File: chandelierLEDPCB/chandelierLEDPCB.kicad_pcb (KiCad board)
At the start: 2 copper layers, 100 x 100 mm, 122 parts, among them J1 JST PH 1x02 SMT VERT, J3 JST PH 1x02 SMT VERT, Q1 Si2301CDS, Q10 Si2301CDS, Q11 Si2301CDS, Q12 Si2301CDS, Q13 Si2301CDS, Q14 Si2301CDS, Q15 Si2301CDS, Q16 Si2301CDS, Q17 Si2301CDS, Q18 Si2301CDS, Q19 Si2301CDS, Q2 Si2301CDS, Q20 Si2301CDS, Q21 Si2301CDS, Q22 Si2301CDS, Q23 Si2301CDS, Q24 Si2301CDS, Q3 Si2301CDS, Q4 Si2301CDS, Q5 Si2301CDS, Q6 Si2301CDS, Q7 Si2301CDS, Q8 Si2301CDS, Q9 Si2301CDS, U1 WS2811, U2 WS2811, U3 WS2811, U4 WS2811, U5 WS2811, U6 WS2811, U7 WS2811, U8 WS2811

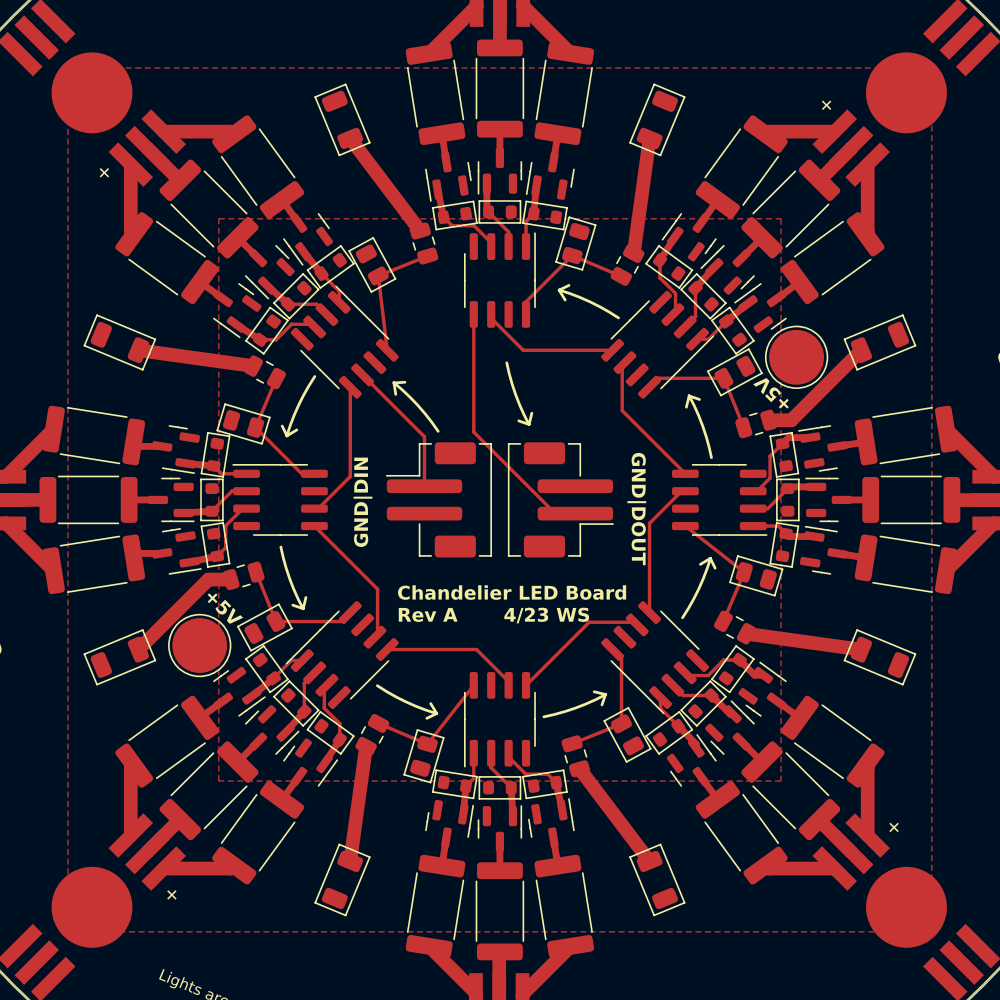
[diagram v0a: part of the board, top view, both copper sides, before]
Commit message: Edited LED to have EP disconnected
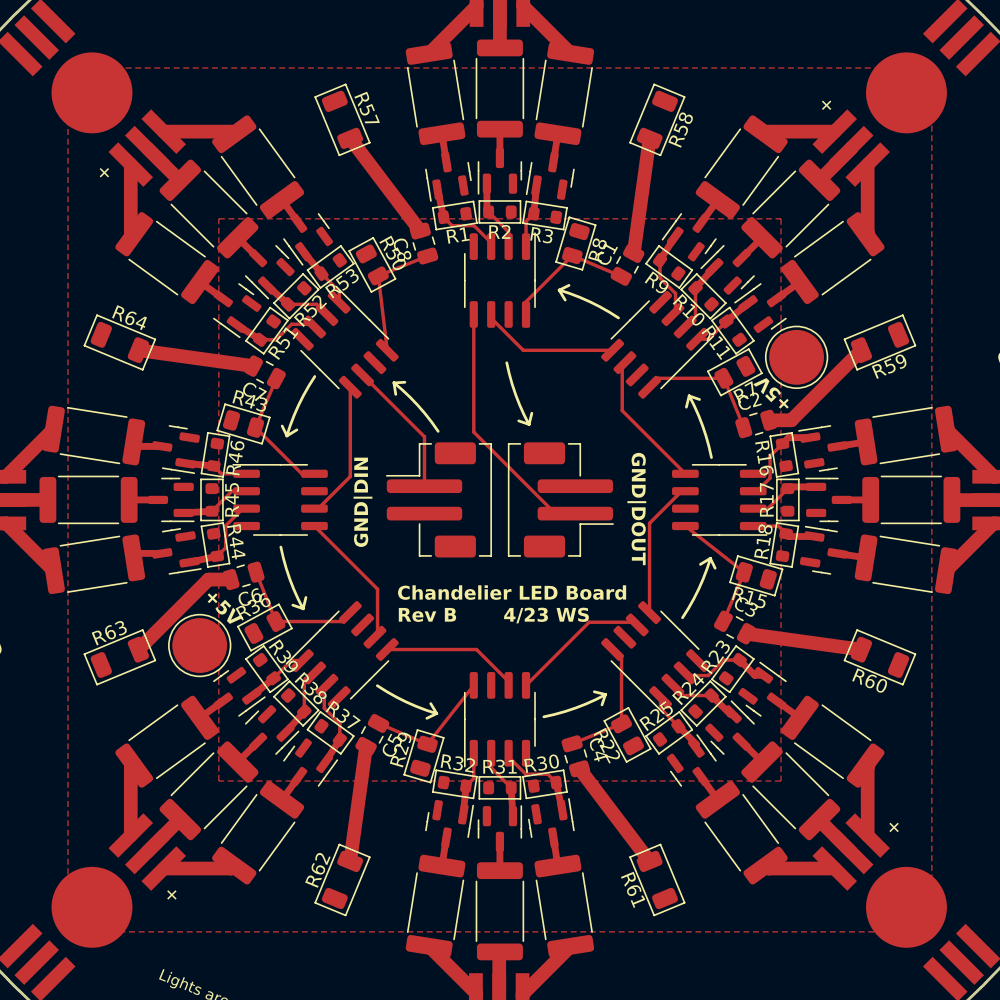
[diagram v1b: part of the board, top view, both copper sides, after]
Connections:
- D1 pad 7: GNDPWR -> unconnected-(D1-PAD-Pad7)
- D2 pad 7: GNDPWR -> unconnected-(D2-PAD-Pad7)
- D3 pad 7: GNDPWR -> unconnected-(D3-PAD-Pad7)
- D4 pad 7: GNDPWR -> unconnected-(D4-PAD-Pad7)
- D5 pad 7: GNDPWR -> unconnected-(D5-PAD-Pad7)
- D6 pad 7: GNDPWR -> unconnected-(D6-PAD-Pad7)
- D7 pad 7: GNDPWR -> unconnected-(D7-PAD-Pad7)
- D8 pad 7: GNDPWR -> unconnected-(D8-PAD-Pad7)
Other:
- board text added: "Chandelier LED Board Rev B 4/23 WS"
- board text removed: "Chandelier LED Board Rev A 4/23 WS"
